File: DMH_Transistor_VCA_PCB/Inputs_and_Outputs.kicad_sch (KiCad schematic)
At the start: 0 parts

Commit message: Finished schematic
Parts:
- added J1, J2, J3, J4, J5, J6, J7, J8: TS_Jack_6.35mm_Sw, SynthStuff:CUI_MJ-63052A, symbol SynthStuff:TS_Jack_6.35mm_Sw
- added J10: Conn_01x04, symbol Connector_Generic:Conn_01x04
- added J200: IDC_02x05, SynthStuff:IDC-Header_2x05_P2.54mm_Vertical_BackBone, symbol SynthStuff:BackBone_Connector_10Pin
- added J50: Conn_01x04, Connector_PinHeader_2.54mm:PinHeader_1x04_P2.54mm_Vertical, symbol Connector_Generic:Conn_01x04
- added RV1, RV2, RV5, RV7: 100k, SynthStuff:Potentiometer_TT_P110KH1, symbol Device:R_Potentiometer_US
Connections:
- new net: J1.TN, J200.1 (Pin_1)
- new net: J2.TN, J200.2 (Pin_2)
- new net: J200.3 (Pin_3), J3.TN
- new net: J200.4 (Pin_4), J4.TN
- new net: J200.6 (Pin_6), J8.TN
- new net: J200.7 (Pin_7), J7.TN
- new net: J200.8 (Pin_8), J6.TN
- new net: J200.9 (Pin_9), J5.TN
- new net CV 1 A Jack: J3.T, RV1.3
- new net CV 1 A Pot: J50.1 (Pin_1), RV1.2
- new net CV 1 B Jack: J7.T, RV5.3
- new net CV 1 B Pot: J10.1 (Pin_1), RV5.2
- new net CV 2 A Jack: J4.T, RV2.3
- new net CV 2 A Pot: J50.2 (Pin_2), RV2.2
- new net CV 2 B Jack: J8.T, RV7.3
- new net CV 2 B Pot: J10.2 (Pin_2), RV7.2
- new net GND: J1.S, J10.3 (Pin_3), J10.4 (Pin_4), J2.S, J200.10 (Pin_10), J200.5 (Pin_5), J3.S, J4.S, J5.S, J50.3 (Pin_3), J50.4 (Pin_4), J6.S, J7.S, J8.S, RV1.1, RV2.1, RV5.1, RV7.1
- new net Input A Jack: J1.T
- new net Input B Jack: J5.T
- new net Output A Jack: J2.T
- new net Output B Jack: J6.T

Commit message: Finished main PCB
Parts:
- added R21, R40: 20k, Resistor_THT:R_Axial_DIN0207_L6.3mm_D2.5mm_P7.62mm_Horizontal, symbol Device:R_US
- added RV3, RV8: 100k, SynthStuff:Potentiometer_Alpha_RD901F-40-00D_Single_Vertical, symbol Device:R_Potentiometer_US
- J50: value Conn_01x04 -> Conn_01x05; footprint Connector_PinHeader_2.54mm:PinHeader_1x04_P2.54mm_Vertical -> Connector_PinSocket_2.54mm:PinSocket_1x05_P2.54mm_Vertical; symbol Connector_Generic:Conn_01x04 -> Connector_Generic:Conn_01x05
- J60: renamed from J10; value Conn_01x04 -> Conn_01x05; footprint (none) -> Connector_PinSocket_2.54mm:PinSocket_1x05_P2.54mm_Vertical; symbol Connector_Generic:Conn_01x04 -> Connector_Generic:Conn_01x05
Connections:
- net CV 1 A Pot: now also J50.2 (Pin_2); no longer J50.1 (Pin_1)
- net CV 1 B Pot: now also J60.2 (Pin_2); no longer J60.1 (Pin_1)
- net CV 2 A Pot: now also J50.3 (Pin_3); no longer J50.2 (Pin_2)
- net CV 2 B Pot: now also J60.3 (Pin_3); no longer J60.2 (Pin_2)
- net GND: now also J50.5 (Pin_5), J60.5 (Pin_5), RV3.1, RV8.1; no longer J50.3 (Pin_3), J60.3 (Pin_3)
- new net: R40.1, RV8.3
- new net: R21.1, RV3.3
- new net +12V: R21.2, R40.2
- new net Offset A Pot: J50.1 (Pin_1), RV3.2
- new net Offset B Pot: J60.1 (Pin_1), RV8.2
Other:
- note added: "Pots PCB"

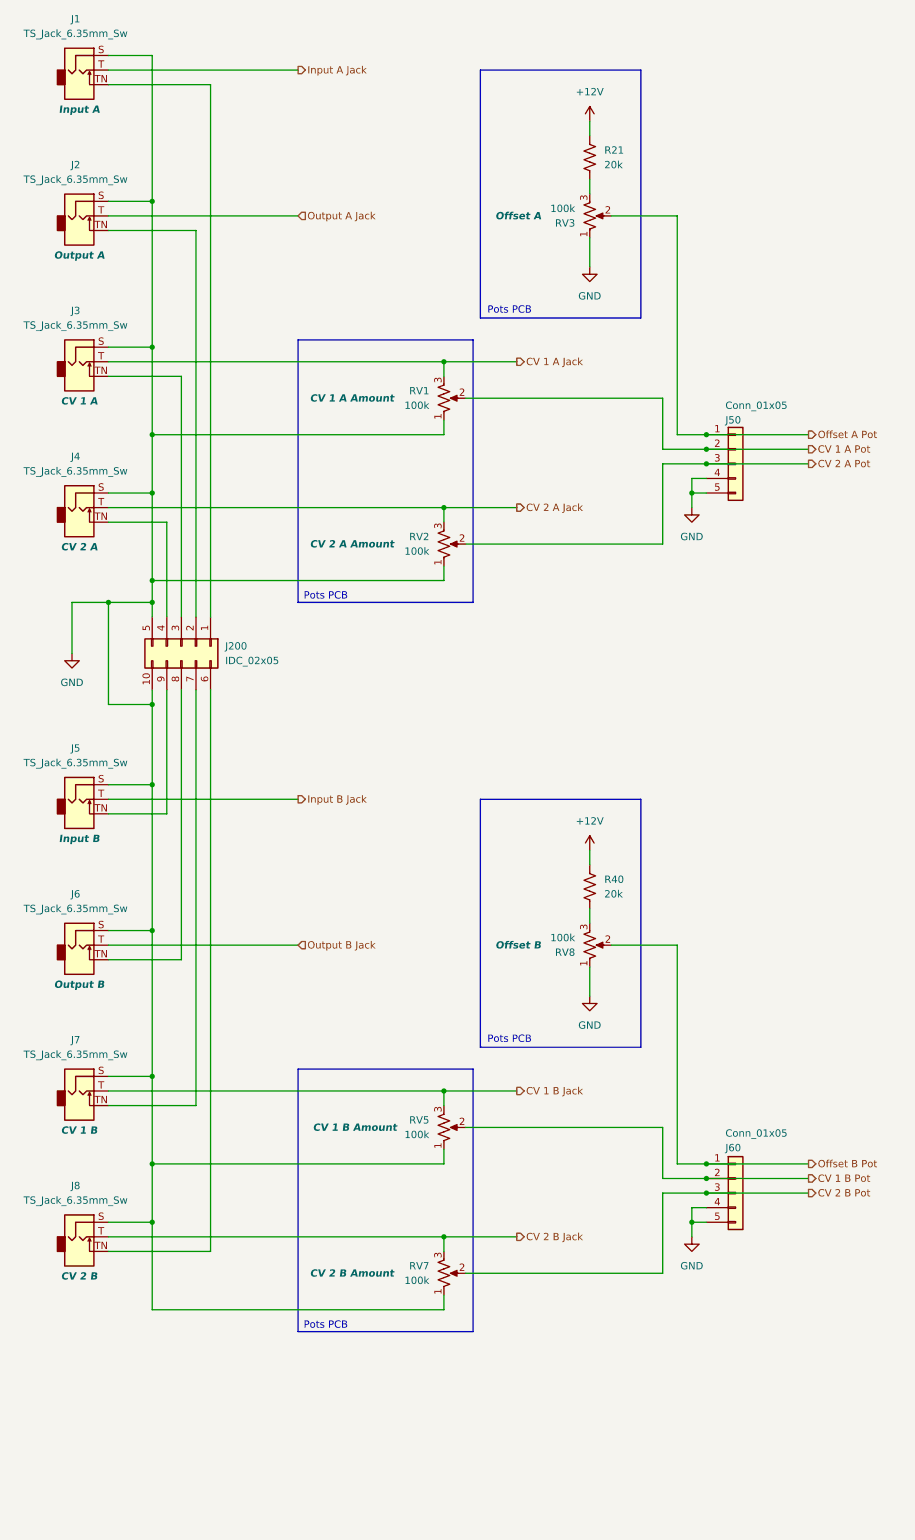
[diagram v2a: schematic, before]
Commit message: Pots PCB in progress
Need to add CV input traces to the pin headers
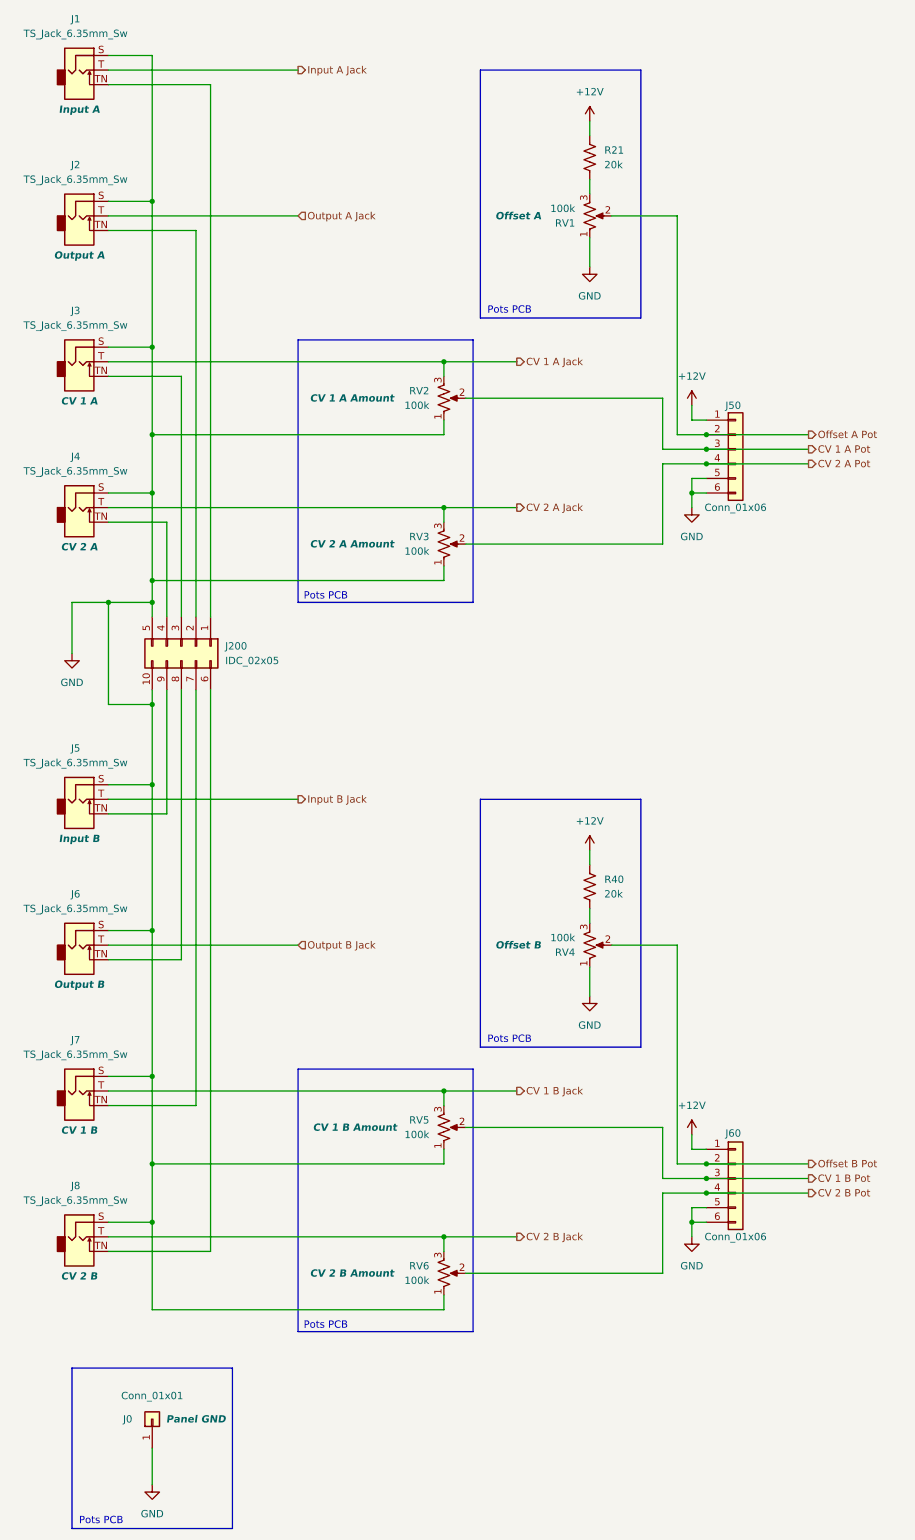
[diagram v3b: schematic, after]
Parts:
- added J0: Conn_01x01, Connector_PinHeader_2.54mm:PinHeader_1x01_P2.54mm_Vertical, symbol Connector_Generic:Conn_01x01
- J50, J60: value Conn_01x05 -> Conn_01x06; footprint Connector_PinSocket_2.54mm:PinSocket_1x05_P2.54mm_Vertical -> Connector_PinSocket_2.54mm:PinSocket_1x06_P2.54mm_Vertical; symbol Connector_Generic:Conn_01x05 -> Connector_Generic:Conn_01x06
- renumbered RV3 to RV1, RV1 to RV2, RV2 to RV3, RV8 to RV4, RV7 to RV6
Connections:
- net +12V: now also J50.1 (Pin_1), J60.1 (Pin_1)
- net CV 1 A Pot: now also J50.3 (Pin_3); no longer J50.2 (Pin_2)
- net CV 1 B Pot: now also J60.3 (Pin_3); no longer J60.2 (Pin_2)
- net CV 2 A Pot: now also J50.4 (Pin_4); no longer J50.3 (Pin_3)
- net CV 2 B Pot: now also J60.4 (Pin_4); no longer J60.3 (Pin_3)
- net GND: now also J50.6 (Pin_6), J60.6 (Pin_6), J0.1 (Pin_1); no longer J50.4 (Pin_4), J60.4 (Pin_4)
- net Offset A Pot: now also J50.2 (Pin_2); no longer J50.1 (Pin_1)
- net Offset B Pot: now also J60.2 (Pin_2); no longer J60.1 (Pin_1)

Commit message: Finished Pots PCB
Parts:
- J50, J60: value Conn_01x06 -> Conn_01x08; footprint Connector_PinSocket_2.54mm:PinSocket_1x06_P2.54mm_Vertical -> Connector_PinSocket_2.54mm:PinSocket_1x08_P2.54mm_Vertical; symbol Connector_Generic:Conn_01x06 -> Connector_Generic:Conn_01x08
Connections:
- net +12V: now also J50.3 (Pin_3), J60.3 (Pin_3); no longer J50.1 (Pin_1), J60.1 (Pin_1)
- net CV 1 A Jack: now also J50.1 (Pin_1)
- net CV 1 A Pot: now also J50.5 (Pin_5); no longer J50.3 (Pin_3)
- net CV 1 B Jack: now also J60.1 (Pin_1)
- net CV 1 B Pot: now also J60.5 (Pin_5); no longer J60.3 (Pin_3)
- net CV 2 A Jack: now also J50.2 (Pin_2)
- net CV 2 A Pot: now also J50.6 (Pin_6); no longer J50.4 (Pin_4)
- net CV 2 B Jack: now also J60.2 (Pin_2)
- net CV 2 B Pot: now also J60.6 (Pin_6); no longer J60.4 (Pin_4)
- net GND: now also J50.7 (Pin_7), J50.8 (Pin_8), J60.7 (Pin_7), J60.8 (Pin_8); no longer J50.5 (Pin_5), J50.6 (Pin_6), J60.5 (Pin_5), J60.6 (Pin_6)
- net Offset A Pot: now also J50.4 (Pin_4); no longer J50.2 (Pin_2)
- net Offset B Pot: now also J60.4 (Pin_4); no longer J60.2 (Pin_2)

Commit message: Switched attenuverters trimpot and Rf positions
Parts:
- J0: now not fitted; now left out of the parts list
- RV2: Function CV 1 A Amount -> CV 1A Amt
- RV3: Function CV 2 A Amount -> CV 2A Amt
- RV5: Function CV 1 B Amount -> CV 1B Amt
- RV6: Function CV 2 B Amount -> CV 2B Amt
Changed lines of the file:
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@@
 			)
 		)
-		(property "Function" "CV 2 A Amount"
+		(property "Function" "CV 2A Amt"
 			(at 72.898 107.95 0)
 			(effects
@@
 		(unit 1)
 		(exclude_from_sim no)
-		(in_bom yes)
+		(in_bom no)
 		(on_board no)
-		(dnp no)
+		(dnp yes)
 		(property "Reference" "J0"
 			(at 33.02 260.35 90)
@@
 			)
 		)
-		(property "Function" "CV 1 B Amount"
+		(property "Function" "CV 1B Amt"
 			(at 73.406 209.55 0)
 			(effects
@@
 			)
 		)
-		(property "Function" "CV 1 A Amount"
+		(property "Function" "CV 1A Amt"
 			(at 72.898 82.55 0)
 			(effects
@@
 			)
 		)
-		(property "Function" "CV 2 B Amount"
+		(property "Function" "CV 2B Amt"
 			(at 72.898 234.95 0)
 			(effects
